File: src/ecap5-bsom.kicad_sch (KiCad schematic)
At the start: 0 parts

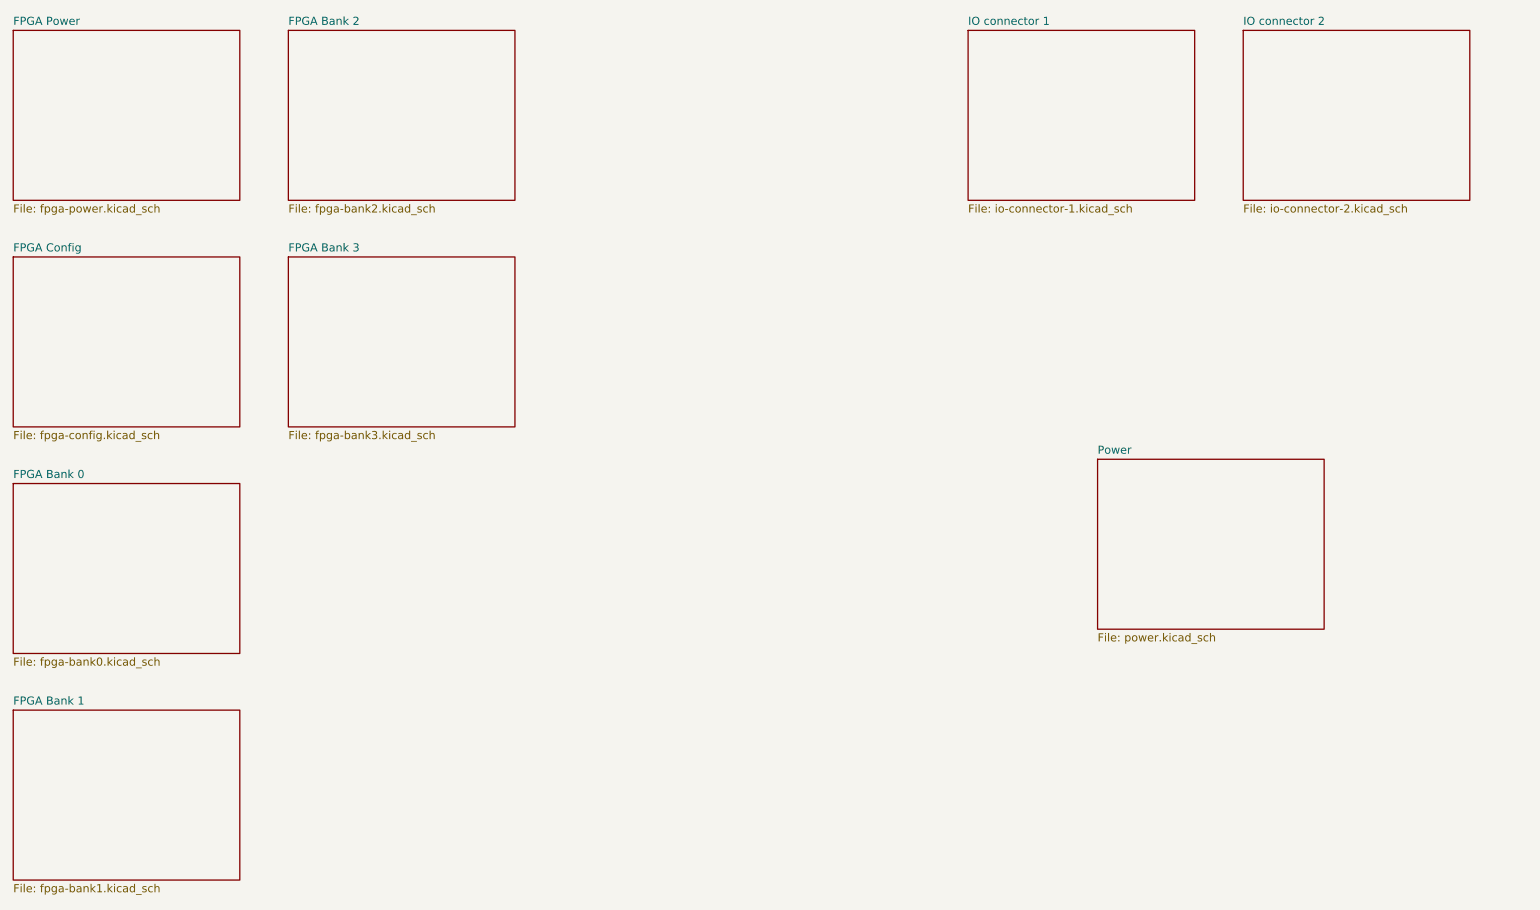
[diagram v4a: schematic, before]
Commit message: Finishes FPGA symbol
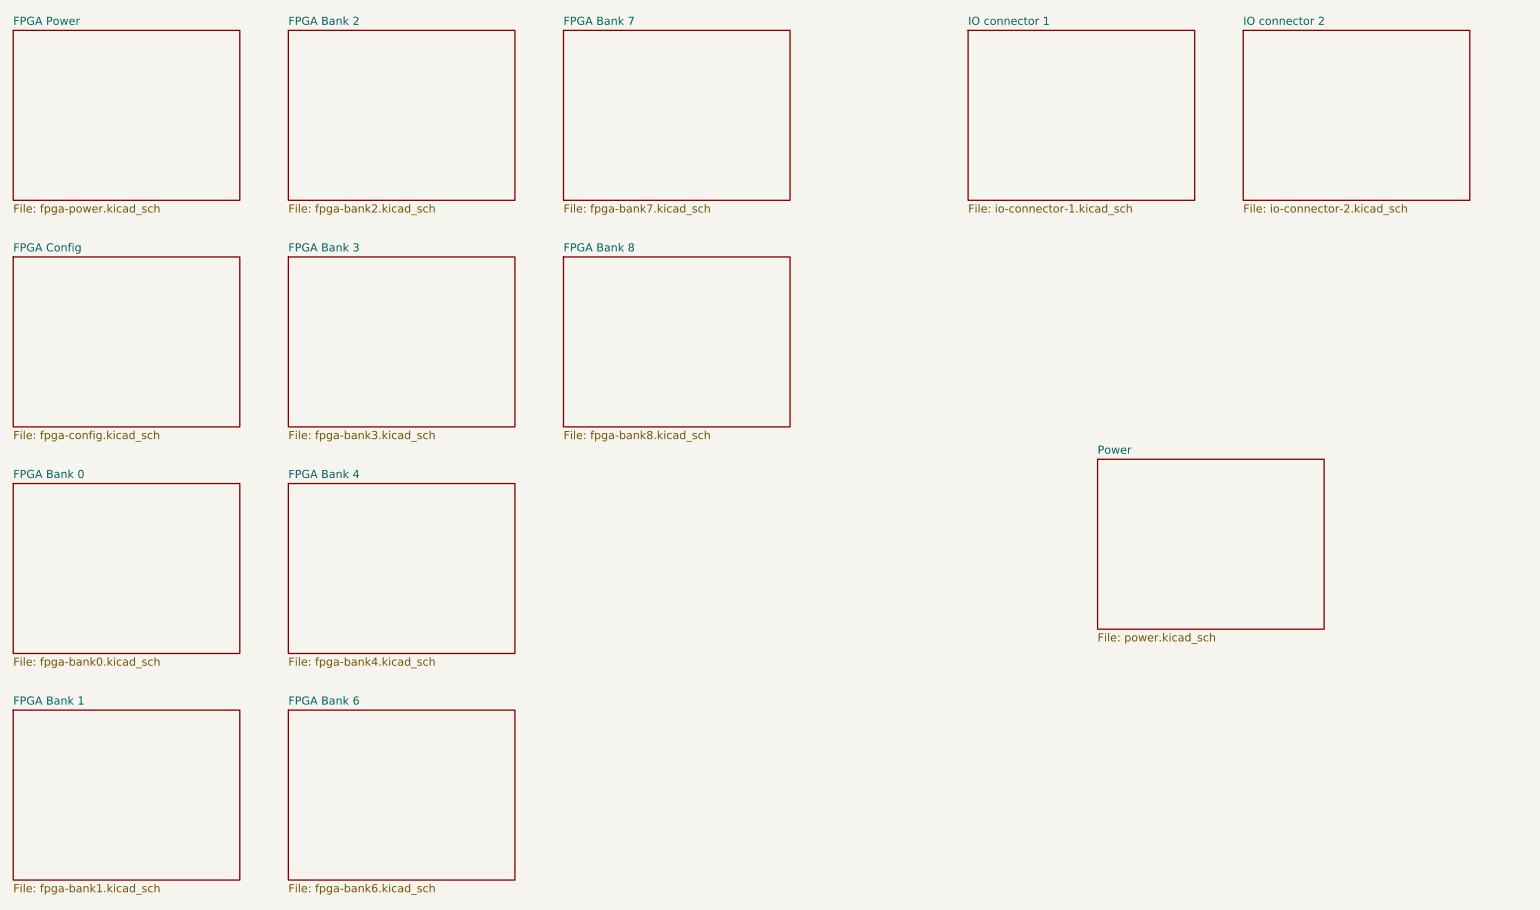
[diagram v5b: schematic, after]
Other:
- added sheet FPGA Bank 4 (fpga-bank4.kicad_sch)
- added sheet FPGA Bank 6 (fpga-bank6.kicad_sch)
- added sheet FPGA Bank 7 (fpga-bank7.kicad_sch)
- added sheet FPGA Bank 8 (fpga-bank8.kicad_sch)
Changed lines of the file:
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@@
+	)
+	(sheet
+		(at 119.38 63.5)
+		(size 35.56 26.67)
+		(fields_autoplaced yes)
+		(stroke
+			(width 0.1524)
+			(type solid)
+		)
+		(fill
+			(color 0 0 0 0.0000)
+		)
+		(property "Sheetname" "FPGA Bank 8"
+			(at 119.38 62.7884 0)
+			(effects
+				(font
+					(size 1.27 1.27)
+				)
+				(justify left bottom)
+			)
+		)
+		(property "Sheetfile" "fpga-bank8.kicad_sch"
+			(at 119.38 90.7546 0)
+			(effects
+				(font
+					(size 1.27 1.27)
+				)
+				(justify left top)
+			)
+		)
+		(instances
+			(project "ecap5-bsom"
+				(path "/c5fd18a3-9aa0-4151-b6e0-94da3d606686"
+					(page "14")
+				)
+			)
+		)
 	)
 	(sheet
@@
 	)
 	(sheet
+		(at 76.2 134.62)
+		(size 35.56 26.67)
+		(fields_autoplaced yes)
+		(stroke
+			(width 0.1524)
+			(type solid)
+		)
+		(fill
+			(color 0 0 0 0.0000)
+		)
+		(property "Sheetname" "FPGA Bank 6"
+			(at 76.2 133.9084 0)
+			(effects
+				(font
+					(size 1.27 1.27)
+				)
+				(justify left bottom)
+			)
+		)
+		(property "Sheetfile" "fpga-bank6.kicad_sch"
+			(at 76.2 161.8746 0)
+			(effects
+				(font
+					(size 1.27 1.27)
+				)
+				(justify left top)
+			)
+		)
+		(instances
+			(project "ecap5-bsom"
+				(path "/c5fd18a3-9aa0-4151-b6e0-94da3d606686"
+					(page "12")
+				)
+			)
+		)
+	)
+	(sheet
 		(at 33.02 27.94)
 		(size 35.56 26.67)
@@
 	)
 	(sheet
+		(at 76.2 99.06)
+		(size 35.56 26.67)
+		(fields_autoplaced yes)
+		(stroke
+			(width 0.1524)
+			(type solid)
+		)
+		(fill
+			(color 0 0 0 0.0000)
+		)
+		(property "Sheetname" "FPGA Bank 4"
+			(at 76.2 98.3484 0)
+			(effects
+				(font
+					(size 1.27 1.27)
+				)
+				(justify left bottom)
+			)
+		)
+		(property "Sheetfile" "fpga-bank4.kicad_sch"
+			(at 76.2 126.3146 0)
+			(effects
+				(font
+					(size 1.27 1.27)
+				)
+				(justify left top)
+			)
+		)
+		(instances
+			(project "ecap5-bsom"
+				(path "/c5fd18a3-9aa0-4151-b6e0-94da3d606686"
+					(page "11")
+				)
+			)
+		)
+	)
+	(sheet
 		(at 33.02 134.62)
 		(size 35.56 26.67)
@@
 				)
 			)
+		)
+	)
+	(sheet
+		(at 119.38 27.94)
+		(size 35.56 26.67)
+		(fields_autoplaced yes)
+		(stroke
+			(width 0.1524)
+			(type solid)
+		)
+		(fill
+			(color 0 0 0 0.0000)
+		)
+		(property "Sheetname" "FPGA Bank 7"
+			(at 119.38 27.2284 0)
+			(effects
+				(font
+					(size 1.27 1.27)
+				)
+				(justify left bottom)
+			)
+		)
+		(property "Sheetfile" "fpga-bank7.kicad_sch"
+			(at 119.38 55.1946 0)
+			(effects
+				(font
+					(size 1.27 1.27)
+				)
+				(justify left top)
+			)
+		)
+		(instances
+			(project "ecap5-bsom"
+				(path "/c5fd18a3-9aa0-4151-b6e0-94da3d606686"
+					(page "13")
+				)
+			)

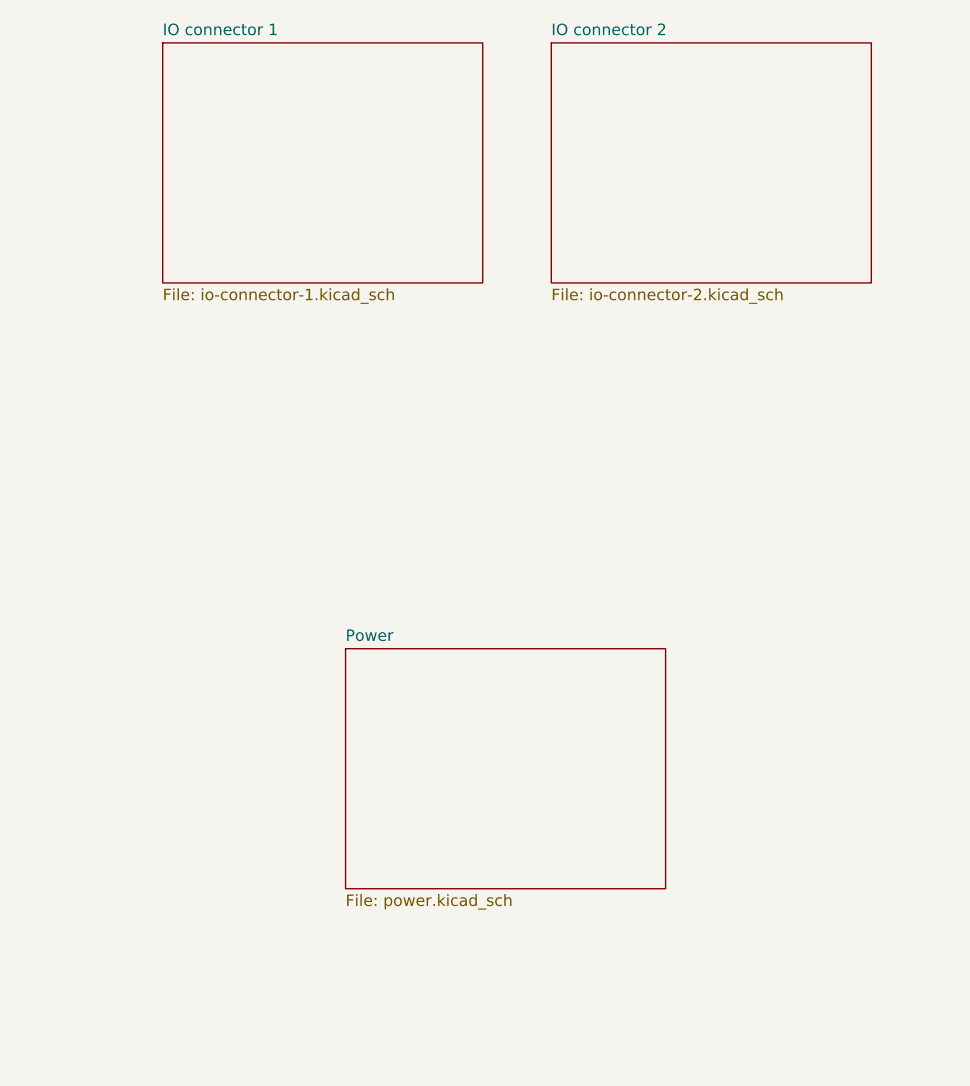
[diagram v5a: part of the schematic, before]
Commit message: Updates the fpga configuration schematic
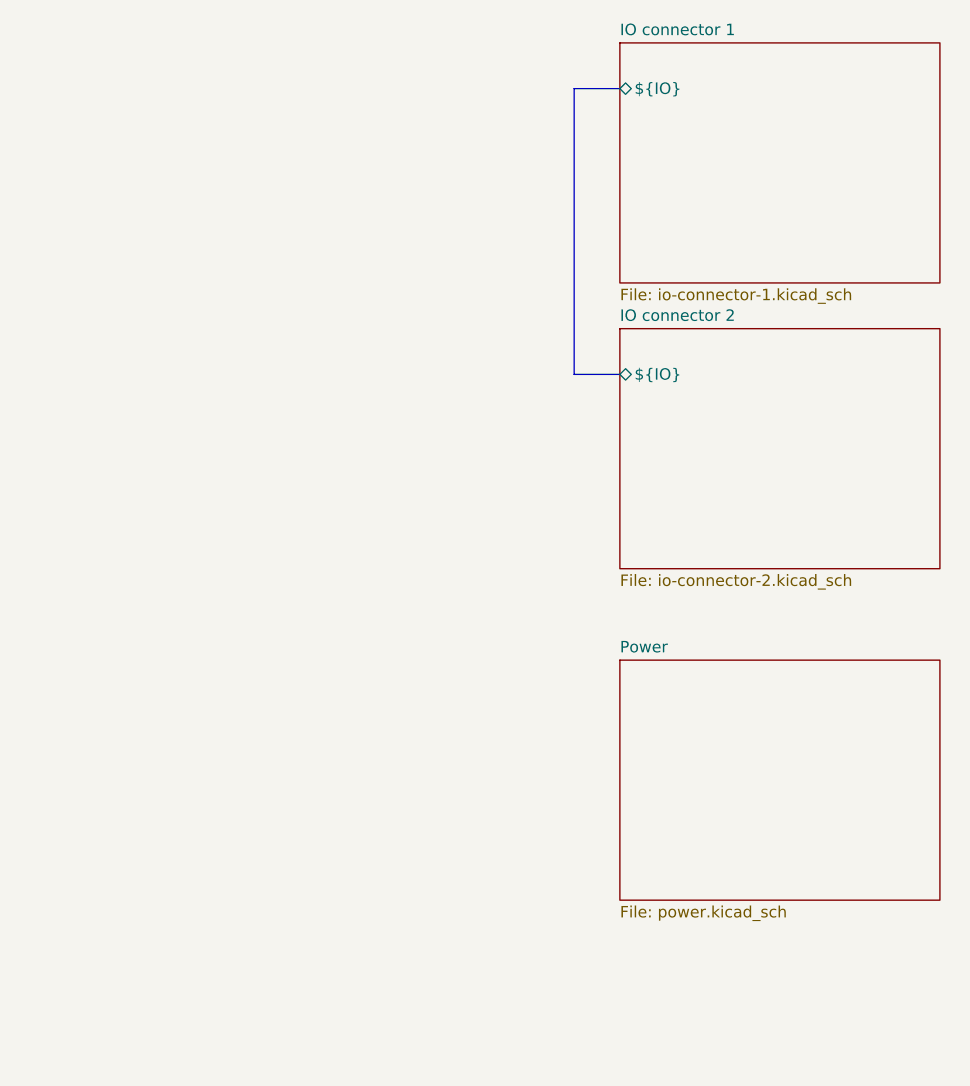
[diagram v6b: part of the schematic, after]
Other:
- sheet IO connector 1 ports: added ${IO}; removed none
- sheet IO connector 2 ports: added ${IO}; removed none
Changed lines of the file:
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@@
 		(comment 3 "${Part Number}")
 	)
-	(sheet
-		(at 226.06 27.94)
+	(bus
+		(pts
+			(xy 228.6 64.77) (xy 233.68 64.77)
+		)
+		(stroke
+			(width 0)
+			(type default)
+		)
+	)
+	(bus
+		(pts
+			(xy 233.68 33.02) (xy 228.6 33.02)
+		)
+		(stroke
+			(width 0)
+			(type default)
+		)
+	)
+	(bus
+		(pts
+			(xy 228.6 33.02) (xy 228.6 64.77)
+		)
+		(stroke
+			(width 0)
+			(type default)
+		)
+	)
+	(sheet
+		(at 233.68 59.69)
 		(size 35.56 26.67)
 		(fields_autoplaced yes)
@@
 		)
 		(property "Sheetname" "IO connector 2"
-			(at 226.06 27.2284 0)
+			(at 233.68 58.9784 0)
 			(effects
 				(font
@@
 		)
 		(property "Sheetfile" "io-connector-2.kicad_sch"
-			(at 226.06 55.1946 0)
-			(effects
-				(font
-					(size 1.27 1.27)
-				)
-				(justify left top)
+			(at 233.68 86.9446 0)
+			(effects
+				(font
+					(size 1.27 1.27)
+				)
+				(justify left top)
+			)
+		)
+		(pin "${IO}" bidirectional
+			(at 233.68 64.77 180)
+			(effects
+				(font
+					(size 1.27 1.27)
+				)
+				(justify left)
 			)
 		)
@@
 	)
 	(sheet
-		(at 182.88 27.94)
+		(at 233.68 27.94)
 		(size 35.56 26.67)
 		(fields_autoplaced yes)
@@
 		)
 		(property "Sheetname" "IO connector 1"
-			(at 182.88 27.2284 0)
+			(at 233.68 27.2284 0)
 			(effects
 				(font
@@
 		)
 		(property "Sheetfile" "io-connector-1.kicad_sch"
-			(at 182.88 55.1946 0)
-			(effects
-				(font
-					(size 1.27 1.27)
-				)
-				(justify left top)
+			(at 233.68 55.1946 0)
+			(effects
+				(font
+					(size 1.27 1.27)
+				)
+				(justify left top)
+			)
+		)
+		(pin "${IO}" bidirectional
+			(at 233.68 33.02 180)
+			(effects
+				(font
+					(size 1.27 1.27)
+				)
+				(justify left)
 			)
 		)
@@
 	)
 	(sheet
-		(at 203.2 95.25)
+		(at 233.68 96.52)
 		(size 35.56 26.67)
 		(fields_autoplaced yes)
@@
 		)
 		(property "Sheetname" "Power"
-			(at 203.2 94.5384 0)
+			(at 233.68 95.8084 0)
 			(effects
 				(font
@@
 		)
 		(property "Sheetfile" "power.kicad_sch"
-			(at 203.2 122.5046 0)
-			(effects
-				(font
+			(at 233.68 123.7746 0)
+			(effects
+				(font

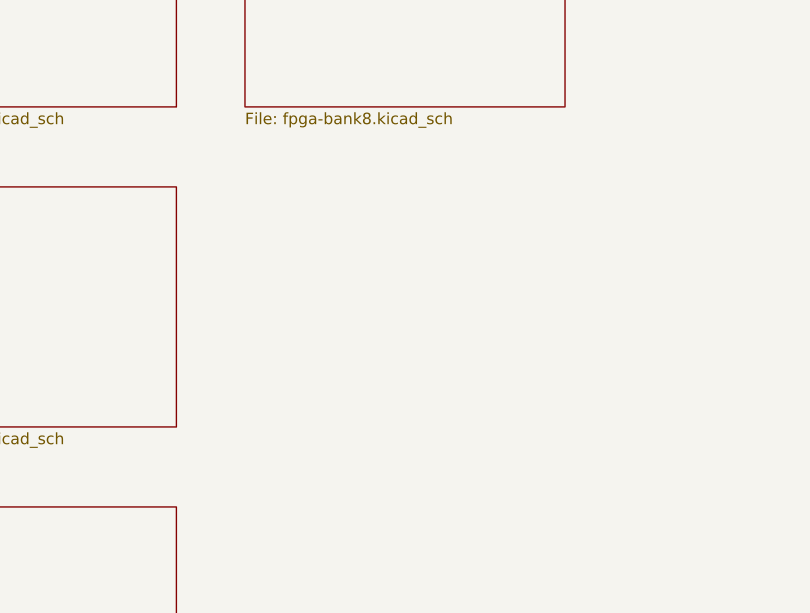
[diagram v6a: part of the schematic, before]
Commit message: Adds SRAM symbol
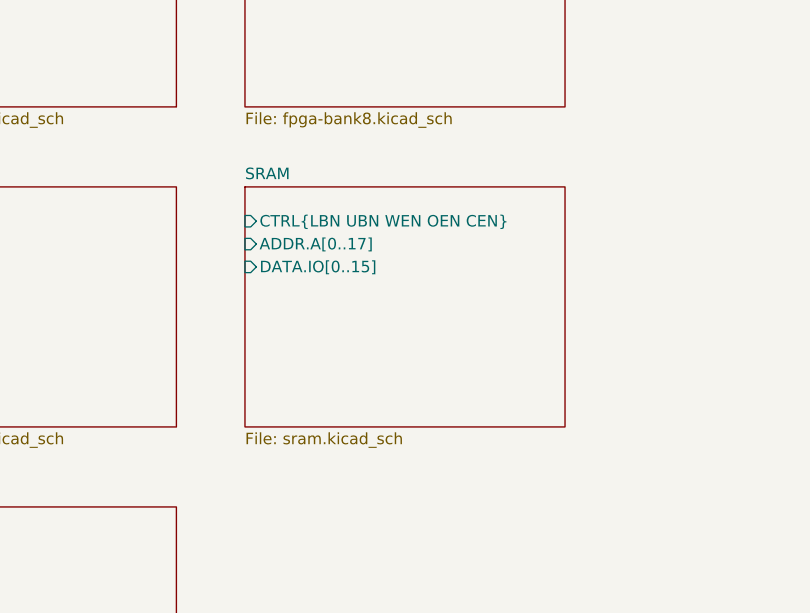
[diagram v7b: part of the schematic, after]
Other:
- added sheet SRAM (sram.kicad_sch)
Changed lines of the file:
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@@
+	)
+	(sheet
+		(at 119.38 99.06)
+		(size 35.56 26.67)
+		(fields_autoplaced yes)
+		(stroke
+			(width 0.1524)
+			(type solid)
+		)
+		(fill
+			(color 0 0 0 0.0000)
+		)
+		(property "Sheetname" "SRAM"
+			(at 119.38 98.3484 0)
+			(effects
+				(font
+					(size 1.27 1.27)
+				)
+				(justify left bottom)
+			)
+		)
+		(property "Sheetfile" "sram.kicad_sch"
+			(at 119.38 126.3146 0)
+			(effects
+				(font
+					(size 1.27 1.27)
+				)
+				(justify left top)
+			)
+		)
+		(pin "CTRL{LBN UBN WEN OEN CEN}" input
+			(at 119.38 102.87 180)
+			(effects
+				(font
+					(size 1.27 1.27)
+				)
+				(justify left)
+			)
+		)
+		(pin "ADDR.A[0..17]" input
+			(at 119.38 105.41 180)
+			(effects
+				(font
+					(size 1.27 1.27)
+				)
+				(justify left)
+			)
+		)
+		(pin "DATA.IO[0..15]" input
+			(at 119.38 107.95 180)
+			(effects
+				(font
+					(size 1.27 1.27)
+				)
+				(justify left)
+			)
+		)
+		(instances
+			(project "ecap5-bsom"
+				(path "/c5fd18a3-9aa0-4151-b6e0-94da3d606686"
+					(page "15")
+				)
+			)
+		)
 	)
 	(sheet

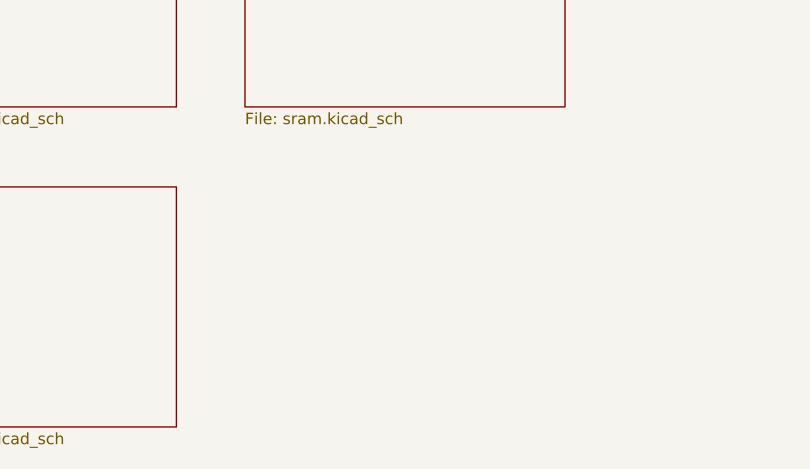
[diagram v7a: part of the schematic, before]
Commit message: Adds DDR symbol
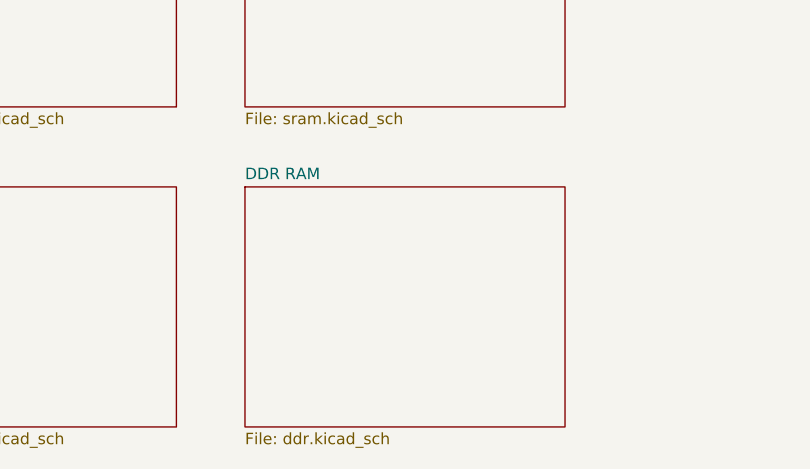
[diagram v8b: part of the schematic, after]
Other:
- added sheet DDR RAM (ddr.kicad_sch)
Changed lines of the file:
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@@
+	)
+	(sheet
+		(at 119.38 134.62)
+		(size 35.56 26.67)
+		(fields_autoplaced yes)
+		(stroke
+			(width 0.1524)
+			(type solid)
+		)
+		(fill
+			(color 0 0 0 0.0000)
+		)
+		(property "Sheetname" "DDR RAM"
+			(at 119.38 133.9084 0)
+			(effects
+				(font
+					(size 1.27 1.27)
+				)
+				(justify left bottom)
+			)
+		)
+		(property "Sheetfile" "ddr.kicad_sch"
+			(at 119.38 161.8746 0)
+			(effects
+				(font
+					(size 1.27 1.27)
+				)
+				(justify left top)
+			)
+		)
+		(instances
+			(project "ecap5-bsom"
+				(path "/c5fd18a3-9aa0-4151-b6e0-94da3d606686"
+					(page "16")
+				)
+			)
+		)
 	)
 	(sheet
